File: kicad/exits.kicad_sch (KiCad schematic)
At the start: 54 parts, among them J1 PJ301M12, J12 Euro power header, J13 PJ301M12, J14 PJ301M12, J2 PJ301M12, J3 PJ301M12, J4 PJ301M12, J5 Attenuator Jumper 1, J6 Attenuator Jumper 2, U1 TL074, U2 RC4580

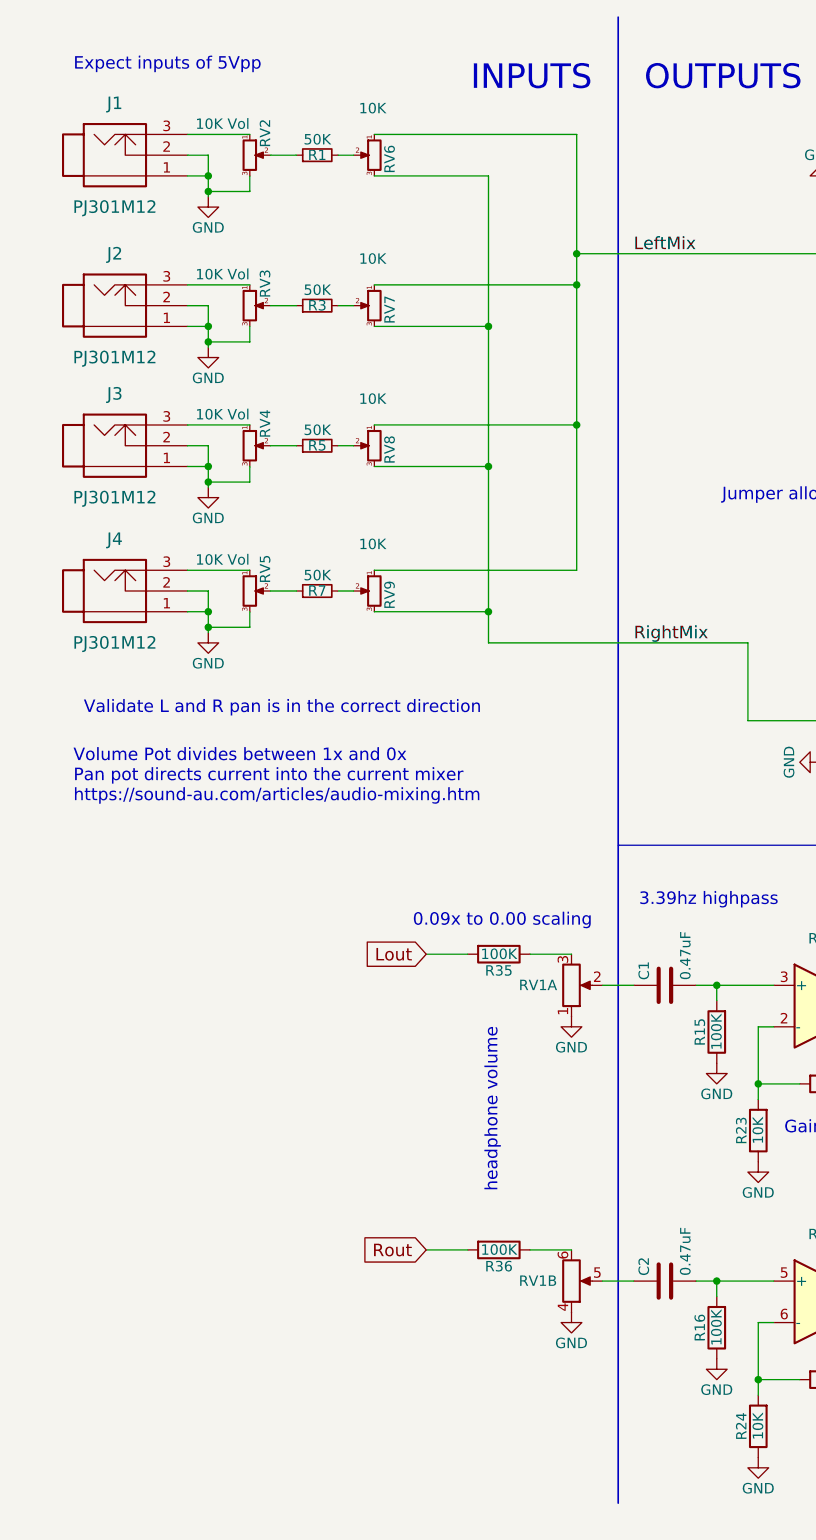
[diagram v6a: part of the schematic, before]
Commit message: Switched L and R channels, so pots all turn the right way
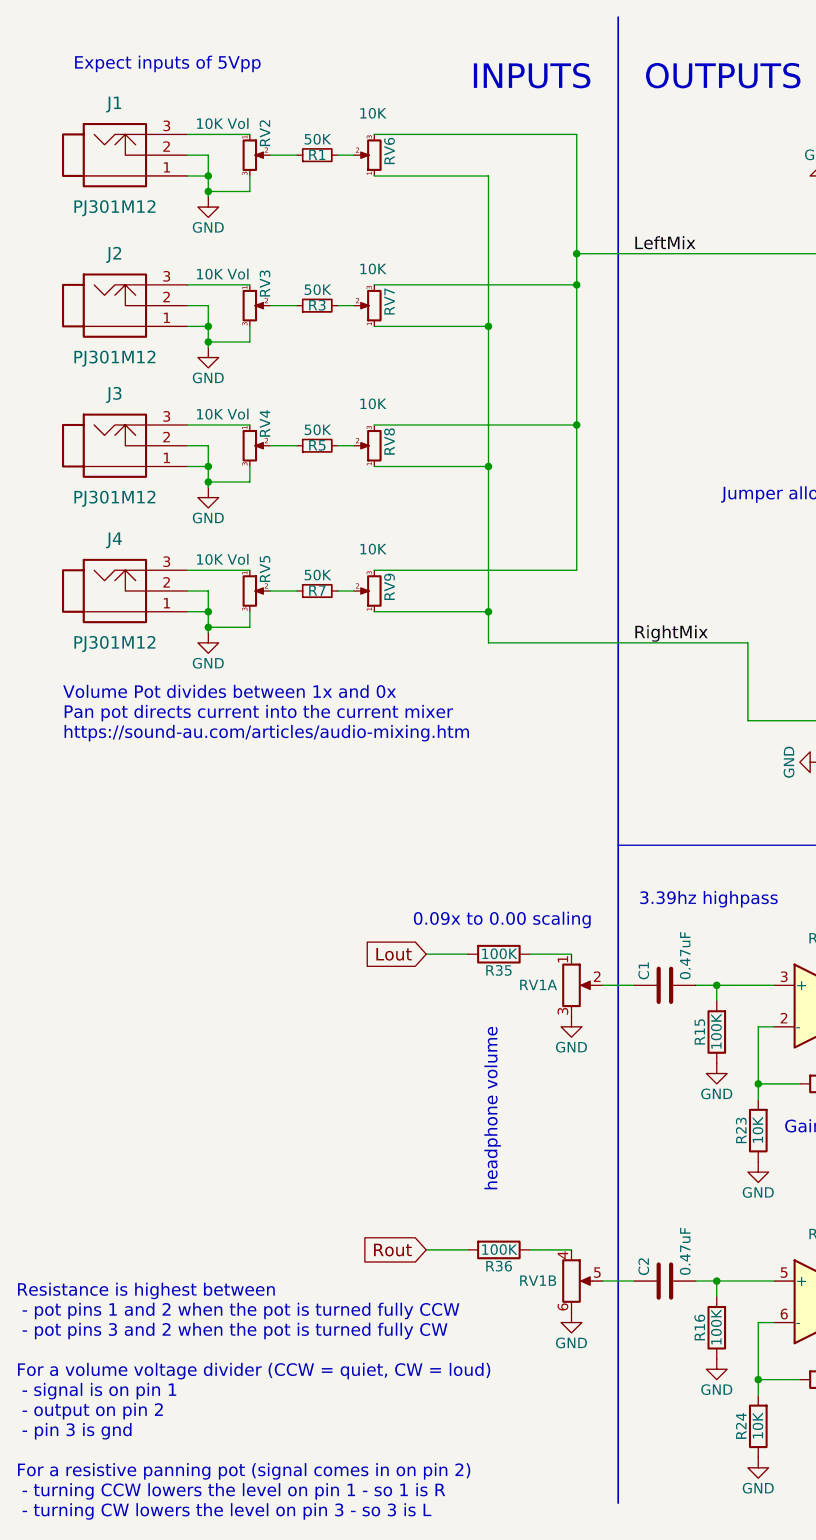
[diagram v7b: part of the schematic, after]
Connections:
- net GND: now also RV1.3, RV1.6; no longer RV1.1, RV1.4
- net LeftMix: now also RV6.3, RV7.3, RV8.3, RV9.3; no longer RV6.1, RV7.1, RV8.1, RV9.1
- net RightMix: now also RV6.1, RV7.1, RV8.1, RV9.1; no longer RV6.3, RV7.3, RV8.3, RV9.3
- net at R36.1: now also RV1.4; no longer RV1.6
- net at R35.1: now also RV1.1; no longer RV1.3
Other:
- note added: "Resistance is highest between - pot pins 1 and 2 when the pot is turned fully CCW - pot pins 3 and 2 when the pot is turned fully CW For a volume voltage divider (CCW = quiet, CW = loud) - signal is on pin 1 - output on pin 2 - pin 3 is gnd For a resistive panning pot (signal comes in on pin 2) - turning CCW lowers the level on pin 1 - so 1 is R - turning CW lowers the level on pin 3 - so 3 is L"
- note removed: "Validate L and R pan is in the correct direction"
- moved on the sheet: RV6, RV7, RV8, RV9
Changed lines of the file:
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@@
   )
   (text "Volume Pot divides between 1x and 0x\nPan pot directs current into the current mixer\nhttps://sound-au.com/articles/audio-mixing.htm"
-    (at 19.685 109.22 0)
+    (at 18.415 101.6 0)
     (effects (font (size 1.524 1.524)) (justify left bottom))
   )
@@
   )
   (text "Gain of 1.1" (at 106.68 149.86 0)
-    (effects (font (size 1.524 1.524)) (justify left bottom))
-  )
-  (text "Validate L and R pan is in the correct direction" (at 20.955 98.425 0)
     (effects (font (size 1.524 1.524)) (justify left bottom))
   )
@@
   )
   (text "power section" (at 242.57 64.516 0)
+    (effects (font (size 1.524 1.524)) (justify left bottom))
+  )
+  (text "Resistance is highest between\n - pot pins 1 and 2 when the pot is turned fully CCW\n - pot pins 3 and 2 when the pot is turned fully CW\n\nFor a volume voltage divider (CCW = quiet, CW = loud)\n - signal is on pin 1\n - output on pin 2\n - pin 3 is gnd\n\nFor a resistive panning pot (signal comes in on pin 2)\n - turning CCW lowers the level on pin 1 - so 1 is R\n - turning CW lowers the level on pin 3 - so 3 is L\n"
+    (at 12.7 196.85 0)
     (effects (font (size 1.524 1.524)) (justify left bottom))
   )
@@
     (pin "2")
   )
-  (symbol (lib_id "Device:R_Potentiometer_Small") (at 56.515 29.845 0) (mirror y) (unit 1)
-    (in_bom yes) (on_board yes)
-    (property "Reference" "RV6" (id 0) (at 58.42 28.575 90)
-      (effects (font (size 1.27 1.27)) (justify right))
-    )
-    (property "Value" "10K" (id 1) (at 54.61 24.13 0)
+  (symbol (lib_id "Device:R_Potentiometer_Small") (at 56.515 29.845 180) (unit 1)
+    (in_bom yes) (on_board yes)
+    (property "Reference" "RV6" (id 0) (at 58.42 31.115 90)
+      (effects (font (size 1.27 1.27)) (justify right))
+    )
+    (property "Value" "10K" (id 1) (at 54.61 24.765 0)
       (effects (font (size 1.27 1.27)) (justify right))
     )
@@
     (pin "2")
   )
-  (symbol (lib_id "Device:R_Potentiometer_Small") (at 56.515 48.26 0) (mirror y) (unit 1)
-    (in_bom yes) (on_board yes)
-    (property "Reference" "RV7" (id 0) (at 58.42 46.99 90)
-      (effects (font (size 1.27 1.27)) (justify right))
-    )
-    (property "Value" "10K" (id 1) (at 54.61 42.545 0)
+  (symbol (lib_id "Device:R_Potentiometer_Small") (at 56.515 48.26 180) (unit 1)
+    (in_bom yes) (on_board yes)
+    (property "Reference" "RV7" (id 0) (at 58.42 49.53 90)
+      (effects (font (size 1.27 1.27)) (justify right))
+    )
+    (property "Value" "10K" (id 1) (at 54.61 43.815 0)
       (effects (font (size 1.27 1.27)) (justify right))
     )
@@
     (pin "1")
   )
-  (symbol (lib_id "Device:R_POT_Dual_Separate") (at 80.645 167.64 0) (mirror x) (unit 2)
+  (symbol (lib_id "Device:R_POT_Dual_Separate") (at 80.645 167.64 0) (unit 2)
     (in_bom yes) (on_board yes)
     (property "Reference" "RV1" (id 0) (at 78.8924 167.64 0)
       (effects (font (size 1.27 1.27)) (justify right))
     )
-    (property "Value" "B10K" (id 1) (at 78.867 166.497 0)
+    (property "Value" "B10K" (id 1) (at 78.867 168.783 0)
       (effects (font (size 1.27 1.27)) (justify right) hide)
     )
@@
     (pin "6")
   )
-  (symbol (lib_id "Device:R_POT_Dual_Separate") (at 80.645 131.445 0) (mirror x) (unit 1)
+  (symbol (lib_id "Device:R_POT_Dual_Separate") (at 80.645 131.445 0) (unit 1)
     (in_bom yes) (on_board yes)
     (property "Reference" "RV1" (id 0) (at 78.8924 131.445 0)
       (effects (font (size 1.27 1.27)) (justify right))
     )
-    (property "Value" "B10K" (id 1) (at 78.867 130.302 0)
+    (property "Value" "B10K" (id 1) (at 78.867 132.588 0)
       (effects (font (size 1.27 1.27)) (justify right) hide)
     )
@@
     (pin "1")
   )
-  (symbol (lib_id "Device:R_Potentiometer_Small") (at 56.515 65.405 0) (mirror y) (unit 1)
-    (in_bom yes) (on_board yes)
-    (property "Reference" "RV8" (id 0) (at 58.42 64.135 90)
-      (effects (font (size 1.27 1.27)) (justify right))
-    )
-    (property "Value" "10K" (id 1) (at 54.61 59.69 0)
+  (symbol (lib_id "Device:R_Potentiometer_Small") (at 56.515 65.405 180) (unit 1)
+    (in_bom yes) (on_board yes)
+    (property "Reference" "RV8" (id 0) (at 58.42 66.675 90)
+      (effects (font (size 1.27 1.27)) (justify right))
+    )
+    (property "Value" "10K" (id 1) (at 54.61 60.325 0)
       (effects (font (size 1.27 1.27)) (justify right))
     )
@@
     (pin "3")
   )
-  (symbol (lib_id "Device:R_Potentiometer_Small") (at 56.515 83.185 0) (mirror y) (unit 1)
-    (in_bom yes) (on_board yes)
-    (property "Reference" "RV9" (id 0) (at 58.42 81.915 90)
-      (effects (font (size 1.27 1.27)) (justify right))
-    )
-    (property "Value" "10K" (id 1) (at 54.61 77.47 0)
-      (effects (font (size 1.27 1.27)) (justify right))
-    )
+  (symbol (lib_id "Device:R_Potentiometer_Small") (at 56.515 83.185 180) (unit 1)
+    (in_bom yes) (on_board yes)
+    (property "Reference" "RV9" (id 0) (at 58.42 84.455 90)
+      (effects (font (size 1.27 1.27)) (justify right))
+    )
+    (property "Value" "10K" (id 1) (at 54.61 78.105 0)
+      (effects (font (size 1.27 1.27)) (justify right))
+    )
